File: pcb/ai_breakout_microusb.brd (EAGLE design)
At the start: 10.2 x 14.2 mm, 4 parts, among them J1 1X04NFNS, J2 1X04NFNS

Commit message: ready for manufacturing
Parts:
- removed U$1: (no value), Ai_Miscellany:AI-LOGO-XS
- added U$2: AI-LOGOXS, Ai_Miscellany:AI-LOGO-XS
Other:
- outline, holes or cut-outs redrawn
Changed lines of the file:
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@@
 <board>
 <plain>
-<wire x1="10.16" y1="0" x2="10.16" y2="14.224" width="0.0254" layer="20"/>
-<wire x1="10.16" y1="14.224" x2="0" y2="14.224" width="0.0254" layer="20"/>
-<wire x1="0" y1="14.224" x2="0" y2="0" width="0.0254" layer="20"/>
-<wire x1="0" y1="0" x2="10.16" y2="0" width="0.0254" layer="20"/>
+<wire x1="0.635" y1="0" x2="9.525" y2="0" width="0.0254" layer="20"/>
+<wire x1="9.525" y1="0" x2="10.16" y2="0.635" width="0.0254" layer="20" curve="90"/>
+<wire x1="10.16" y1="0.635" x2="10.16" y2="13.589" width="0.0254" layer="20"/>
+<wire x1="10.16" y1="13.589" x2="9.525" y2="14.224" width="0.0254" layer="20" curve="90"/>
+<wire x1="9.525" y1="14.224" x2="0.635" y2="14.224" width="0.0254" layer="20"/>
+<wire x1="0.635" y1="14.224" x2="0" y2="13.589" width="0.0254" layer="20" curve="90"/>
+<wire x1="0" y1="13.589" x2="0" y2="0.635" width="0.0254" layer="20"/>
+<wire x1="0" y1="0.635" x2="0.635" y2="0" width="0.0254" layer="20" curve="90"/>
 <text x="6.731" y="12.7" size="1.27" layer="26" font="vector" ratio="10" rot="MR0">GND</text>
 <text x="6.223" y="10.16" size="1.27" layer="26" font="vector" ratio="10" rot="MR0">D+</text>
@@
 </autorouter>
 <elements>
-<element name="U$1" library="Ai_Miscellany" package="AI-LOGO-XS" value="" x="6.477" y="0.889" rot="MR0"/>
 <element name="J1" library="Ai_Connectors" package="1X04-NFNS" value="1X04NFNS" x="1.27" y="9.144" smashed="yes" rot="R90"/>
 <element name="J2" library="Ai_Connectors" package="1X04-NFNS" value="1X04NFNS" x="8.89" y="9.144" smashed="yes" rot="R90"/>
 <element name="USB1" library="Ai_Connectors" package="USB-MICROB-TH" value="USBMICROB-TH" x="5.08" y="1.27"/>
+<element name="U$2" library="Ai_Miscellany" package="AI-LOGO-XS" value="AI-LOGOXS" x="6.477" y="0.635" rot="MR0"/>
 </elements>
 <signals>

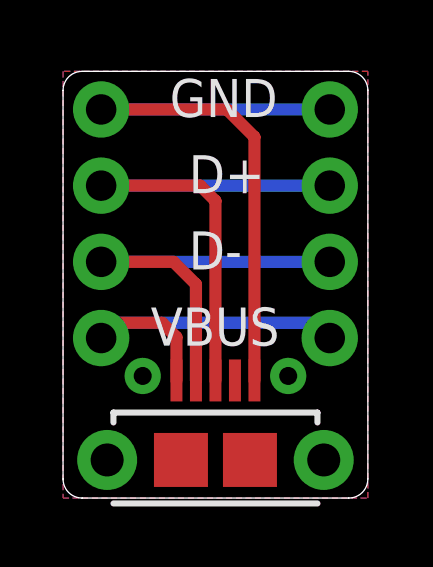
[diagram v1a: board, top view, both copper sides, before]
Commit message: udpated to 2-pin version
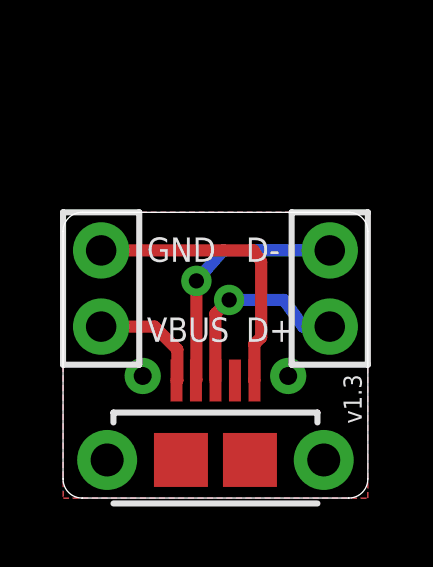
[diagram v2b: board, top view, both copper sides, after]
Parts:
- J1: value 1X04NFNS -> 1X02; device Ai_Connectors:1X04-NFNS -> Ai_Connectors:1X02
- J2: value 1X04NFNS -> 1X02NOFIRST; device Ai_Connectors:1X04-NFNS -> Ai_Connectors:1X02-NOFIRST
- moved J1 2.16 mm to (1.27, 6.99)
- moved J2 2.16 mm to (8.89, 6.99)
- moved U$2 1.14 mm to (6.48, 1.78)
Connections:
- net D+: now also J2.1; no longer J1.3, J2.3
- net D-: no longer J1.2
- net GND: now also J1.2; no longer J1.4, J2.4
- net VBUS: no longer J2.1
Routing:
- net GND: track 21.2 -> 9.59 mm
- net D+: track 17.6 -> 6.68 mm, vias 0 -> 1
- net VBUS: track 12.4 -> 3.92 mm
- net D-: track 14.3 -> 8.23 mm, vias 0 -> 1
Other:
- board size 10.2 x 14.2 mm -> 10.2 x 9.5 mm
- board text added: "v1.3"
- board text removed: "Pasadena, CA"
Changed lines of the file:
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@@
 <?xml version="1.0" encoding="utf-8"?>
 <!DOCTYPE eagle SYSTEM "eagle.dtd">
-<eagle version="7.1.0">
+<eagle version="6.5.0">
 <drawing>
 <settings>
@@
 <wire x1="0.635" y1="0" x2="9.525" y2="0" width="0.0254" layer="20"/>
 <wire x1="9.525" y1="0" x2="10.16" y2="0.635" width="0.0254" layer="20" curve="90"/>
-<wire x1="10.16" y1="0.635" x2="10.16" y2="13.589" width="0.0254" layer="20"/>
-<wire x1="10.16" y1="13.589" x2="9.525" y2="14.224" width="0.0254" layer="20" curve="90"/>
-<wire x1="9.525" y1="14.224" x2="0.635" y2="14.224" width="0.0254" layer="20"/>
-<wire x1="0.635" y1="14.224" x2="0" y2="13.589" width="0.0254" layer="20" curve="90"/>
-<wire x1="0" y1="13.589" x2="0" y2="0.635" width="0.0254" layer="20"/>
+<wire x1="10.16" y1="0.635" x2="10.16" y2="8.89" width="0.0254" layer="20"/>
+<wire x1="10.16" y1="8.89" x2="9.525" y2="9.525" width="0.0254" layer="20" curve="90"/>
+<wire x1="9.525" y1="9.525" x2="0.635" y2="9.525" width="0.0254" layer="20"/>
+<wire x1="0.635" y1="9.525" x2="0" y2="8.89" width="0.0254" layer="20" curve="90"/>
+<wire x1="0" y1="8.89" x2="0" y2="0.635" width="0.0254" layer="20"/>
 <wire x1="0" y1="0.635" x2="0.635" y2="0" width="0.0254" layer="20" curve="90"/>
-<text x="6.731" y="12.7" size="1.27" layer="26" font="vector" ratio="10" rot="MR0">GND</text>
-<text x="6.223" y="10.16" size="1.27" layer="26" font="vector" ratio="10" rot="MR0">D+</text>
-<text x="3.556" y="12.7" size="1.27" layer="25" font="vector" ratio="10" rot="SR0">GND</text>
-<text x="4.191" y="10.16" size="1.27" layer="25" font="vector" ratio="10" rot="SR0">D+</text>
-<text x="6.223" y="7.62" size="1.27" layer="26" font="vector" ratio="10" rot="MR0">D-</text>
-<text x="4.191" y="7.62" size="1.27" layer="25" font="vector" ratio="10" rot="SR0">D-</text>
-<text x="7.747" y="13.081" size="0.6096" layer="26" font="vector" ratio="10" rot="SMR270">Pasadena, CA</text>
-<text x="2.921" y="5.08" size="1.27" layer="25" font="vector" ratio="10" rot="SR0">VBUS</text>
-<text x="7.239" y="5.08" size="1.27" layer="26" font="vector" ratio="10" rot="MR0">VBUS</text>
-<text x="3.048" y="10.16" size="0.6096" layer="26" font="vector" ratio="10" rot="SMR270" align="center">Micro-USB
+<text x="4.826" y="7.874" size="0.8128" layer="26" font="vector" ratio="10" rot="SMR0">GND</text>
+<text x="7.366" y="5.207" size="0.8128" layer="26" font="vector" ratio="10" rot="MR0">D+</text>
+<text x="2.794" y="7.874" size="0.8128" layer="25" font="vector" ratio="10" rot="SR0">GND</text>
+<text x="6.096" y="5.207" size="0.8128" layer="25" font="vector" ratio="10" rot="SR0">D+</text>
+<text x="7.366" y="7.874" size="0.8128" layer="26" font="vector" ratio="10" rot="MR0">D-</text>
+<text x="6.096" y="7.874" size="0.8128" layer="25" font="vector" ratio="10" rot="SR0">D-</text>
+<text x="2.794" y="5.207" size="0.8128" layer="25" font="vector" ratio="10" rot="SR0">VBUS</text>
+<text x="5.588" y="5.207" size="0.8128" layer="26" font="vector" ratio="10" rot="SMR0">VBUS</text>
+<text x="5.08" y="1.016" size="0.6096" layer="26" font="vector" ratio="10" rot="SMR0" align="center">Micro-USB
 Breakout</text>
+<text x="9.652" y="3.302" size="0.6096" layer="25" font="vector" ratio="10" rot="SR90" align="center">v1.3</text>
 </plain>
 <attributes>
@@
 <pass name="Default">
 <param name="RoutingGrid" value="50mil"/>
-<param name="AutoGrid" value="1"/>
-<param name="Efforts" value="0"/>
-<param name="TopRouterVariant" value="1"/>
 <param name="tpViaShape" value="round"/>
-<param name="PrefDir.1" value="a"/>
+<param name="PrefDir.1" value="|"/>
 <param name="PrefDir.2" value="0"/>
 <param name="PrefDir.3" value="0"/>
@@
 <param name="PrefDir.14" value="0"/>
 <param name="PrefDir.15" value="0"/>
-<param name="PrefDir.16" value="a"/>
+<param name="PrefDir.16" value="-"/>
 <param name="cfVia" value="8"/>
 <param name="cfNonPref" value="5"/>
@@
 </autorouter>
 <elements>
-<element name="J1" library="Ai_Connectors" package="1X04-NFNS" value="1X04NFNS" x="1.27" y="9.144" smashed="yes" rot="R90"/>
-<element name="J2" library="Ai_Connectors" package="1X04-NFNS" value="1X04NFNS" x="8.89" y="9.144" smashed="yes" rot="R90"/>
 <element name="USB1" library="Ai_Connectors" package="USB-MICROB-TH" value="USBMICROB-TH" x="5.08" y="1.27"/>
-<element name="U$2" library="Ai_Miscellany" package="AI-LOGO-XS" value="AI-LOGOXS" x="6.477" y="0.635" rot="MR0"/>
+<element name="U$2" library="Ai_Miscellany" package="AI-LOGO-XS" value="AI-LOGOXS" x="6.477" y="1.778" rot="MR0"/>
+<element name="J1" library="Ai_Connectors" package="1X02" value="1X02" x="1.27" y="6.985" smashed="yes" rot="R90"/>
+<element name="J2" library="Ai_Connectors" package="1X02-NOFIRST" value="1X02NOFIRST" x="8.89" y="6.985" smashed="yes" rot="R90"/>
 </elements>
 <signals>
@@
 <polygon width="0.254" layer="16">
 <vertex x="10.16" y="0"/>
-<vertex x="10.16" y="14.224"/>
-<vertex x="0" y="14.224"/>
+<vertex x="10.16" y="9.525"/>
+<vertex x="0" y="9.525"/>
 <vertex x="0" y="0"/>
 </polygon>
 <polygon width="0.254" layer="1">
 <vertex x="10.16" y="0"/>
-<vertex x="10.16" y="14.224"/>
-<vertex x="0" y="14.224"/>
+<vertex x="10.16" y="9.525"/>
+<vertex x="0" y="9.525"/>
 <vertex x="0" y="0"/>
 </polygon>
-<contactref element="J1" pad="4"/>
 <contactref element="USB1" pad="GND"/>
-<contactref element="J2" pad="4"/>
-<wire x1="8.89" y1="12.954" x2="1.27" y2="12.954" width="0.4064" layer="16"/>
-<wire x1="6.38" y1="3.92" x2="6.38" y2="12.035" width="0.4064" layer="1"/>
-<wire x1="6.38" y1="12.035" x2="5.461" y2="12.954" width="0.4064" layer="1"/>
-<wire x1="5.461" y1="12.954" x2="1.27" y2="12.954" width="0.4064" layer="1"/>
+<contactref element="J1" pad="2"/>
+<wire x1="6.3754" y1="5.1308" x2="6.604" y2="5.3594" width="0.4064" layer="1"/>
+<wire x1="6.604" y1="5.3594" x2="6.604" y2="7.874" width="0.4064" layer="1"/>
+<wire x1="6.604" y1="7.874" x2="6.35" y2="8.255" width="0.4064" layer="1"/>
+<wire x1="6.35" y1="8.255" x2="1.27" y2="8.255" width="0.4064" layer="1"/>
+<wire x1="6.38" y1="3.92" x2="6.3754" y2="3.9246" width="0.4064" layer="1"/>
+<wire x1="6.3754" y1="3.9246" x2="6.3754" y2="5.1308" width="0.4064" layer="1"/>
 </signal>
 <signal name="VBUS">
 <contactref element="USB1" pad="VBUS"/>
-<contactref element="J2" pad="1"/>
 <contactref element="J1" pad="1"/>
-<wire x1="8.89" y1="5.334" x2="8.382" y2="5.842" width="0.4064" layer="16"/>
-<wire x1="8.382" y1="5.842" x2="1.778" y2="5.842" width="0.4064" layer="16"/>
-<wire x1="1.778" y1="5.842" x2="1.27" y2="5.334" width="0.4064" layer="16"/>
-<wire x1="3.78" y1="3.92" x2="3.78" y2="5.364" width="0.4064" layer="1"/>
-<wire x1="3.78" y1="5.364" x2="3.302" y2="5.842" width="0.4064" layer="1"/>
-<wire x1="3.302" y1="5.842" x2="1.778" y2="5.842" width="0.4064" layer="1"/>
-<wire x1="1.778" y1="5.842" x2="1.27" y2="5.334" width="0.4064" layer="1"/>
+<wire x1="3.78" y1="3.92" x2="3.81" y2="3.92" width="0.4064" layer="1"/>
+<wire x1="3.81" y1="3.92" x2="3.81" y2="4.953" width="0.4064" layer="1"/>
+<wire x1="3.81" y1="4.953" x2="3.048" y2="5.715" width="0.4064" layer="1"/>
+<wire x1="3.048" y1="5.715" x2="1.27" y2="5.715" width="0.4064" layer="1"/>
 </signal>
 <signal name="D-">
 <contactref element="USB1" pad="D-"/>
 <contactref element="J2" pad="2"/>
-<contactref element="J1" pad="2"/>
-<wire x1="8.89" y1="7.874" x2="1.27" y2="7.874" width="0.4064" layer="16"/>
-<wire x1="4.43" y1="3.92" x2="4.43" y2="7.127" width="0.4064" layer="1"/>
-<wire x1="4.43" y1="7.127" x2="3.683" y2="7.874" width="0.4064" layer="1"/>
-<wire x1="3.683" y1="7.874" x2="1.27" y2="7.874" width="0.4064" layer="1"/>
+<wire x1="4.43" y1="3.92" x2="4.445" y2="3.935" width="0.4064" layer="1"/>
+<wire x1="4.445" y1="3.935" x2="4.445" y2="7.239" width="0.4064" layer="1"/>
+<via x="4.445" y="7.239" extent="1-16" drill="0.508"/>
+<wire x1="4.445" y1="7.239" x2="5.334" y2="8.255" width="0.4064" layer="16"/>
+<wire x1="5.334" y1="8.255" x2="8.89" y2="8.255" width="0.4064" layer="16"/>
 </signal>
 <signal name="D+">
-<contactref element="J2" pad="3"/>
 <contactref element="USB1" pad="D+"/>
-<contactref element="J1" pad="3"/>
-<wire x1="8.89" y1="10.414" x2="1.27" y2="10.414" width="0.4064" layer="16"/>
-<wire x1="5.08" y1="3.92" x2="5.08" y2="9.906" width="0.4064" layer="1"/>
-<wire x1="5.08" y1="9.906" x2="4.572" y2="10.414" width="0.4064" layer="1"/>
-<wire x1="4.572" y1="10.414" x2="1.27" y2="10.414" width="0.4064" layer="1"/>
+<contactref element="J2" pad="1"/>
+<wire x1="5.08" y1="3.92" x2="5.08" y2="6.1468" width="0.4064" layer="1"/>
+<wire x1="5.08" y1="6.1468" x2="5.5372" y2="6.604" width="0.4064" layer="1"/>
+<via x="5.5372" y="6.604" extent="1-16" drill="0.508"/>
+<wire x1="5.5372" y1="6.604" x2="7.366" y2="6.604" width="0.4064" layer="16"/>
+<wire x1="7.366" y1="6.604" x2="8.001" y2="5.715" width="0.4064" layer="16"/>
+<wire x1="8.001" y1="5.715" x2="8.89" y2="5.715" width="0.4064" layer="16"/>
 </signal>
 </signals>
